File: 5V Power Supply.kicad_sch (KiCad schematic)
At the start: 17 parts, among them Q1 CSD13202Q2, U1 TPS61287RZPR

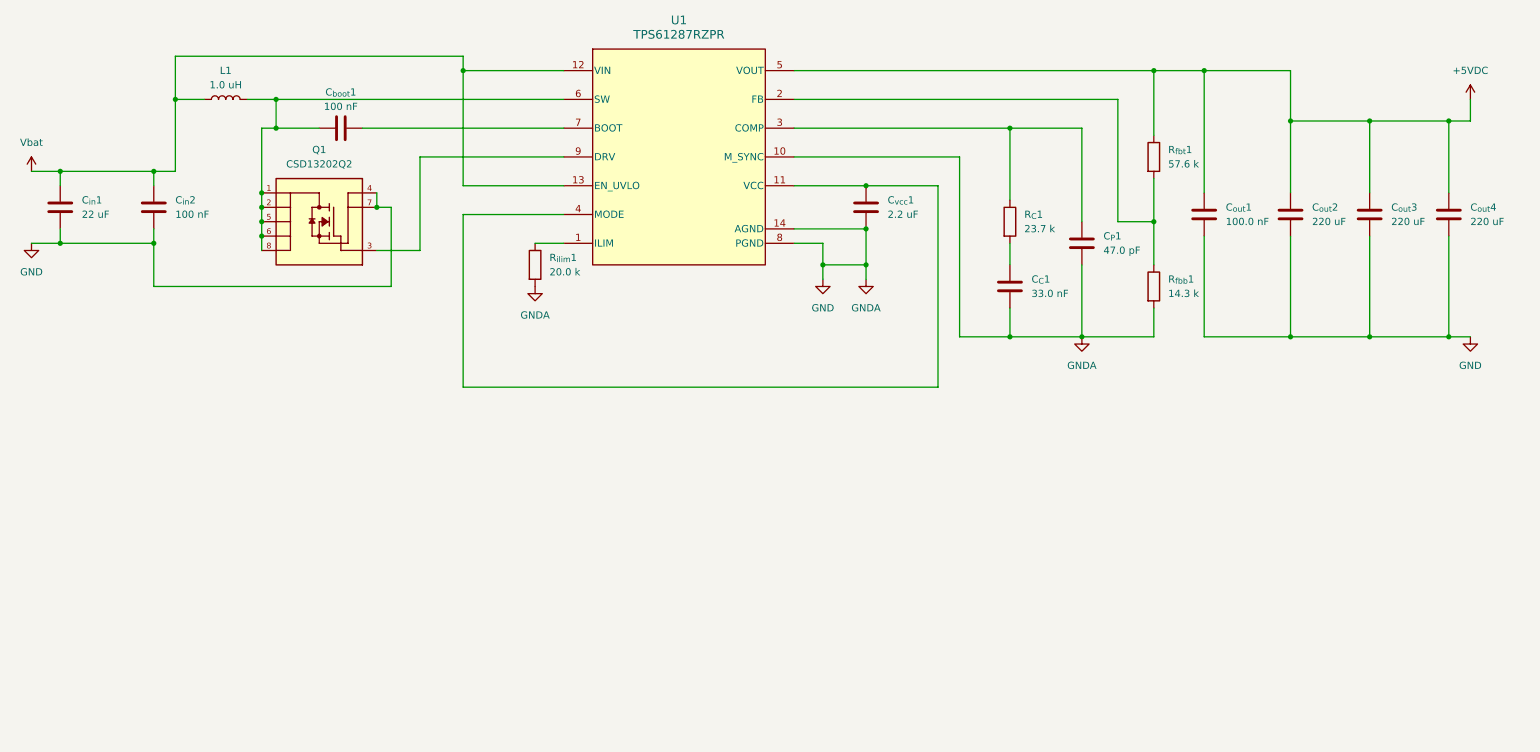
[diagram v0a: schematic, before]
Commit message: feat: Mounting holes, power connectors
Added 2.54 mm ID mounting holes and 4 power connectors. Phoenix Contact spring loaded, good to 16 A, 14-26 AWG wire. 1x on power input from batt, 3x on +5V output.
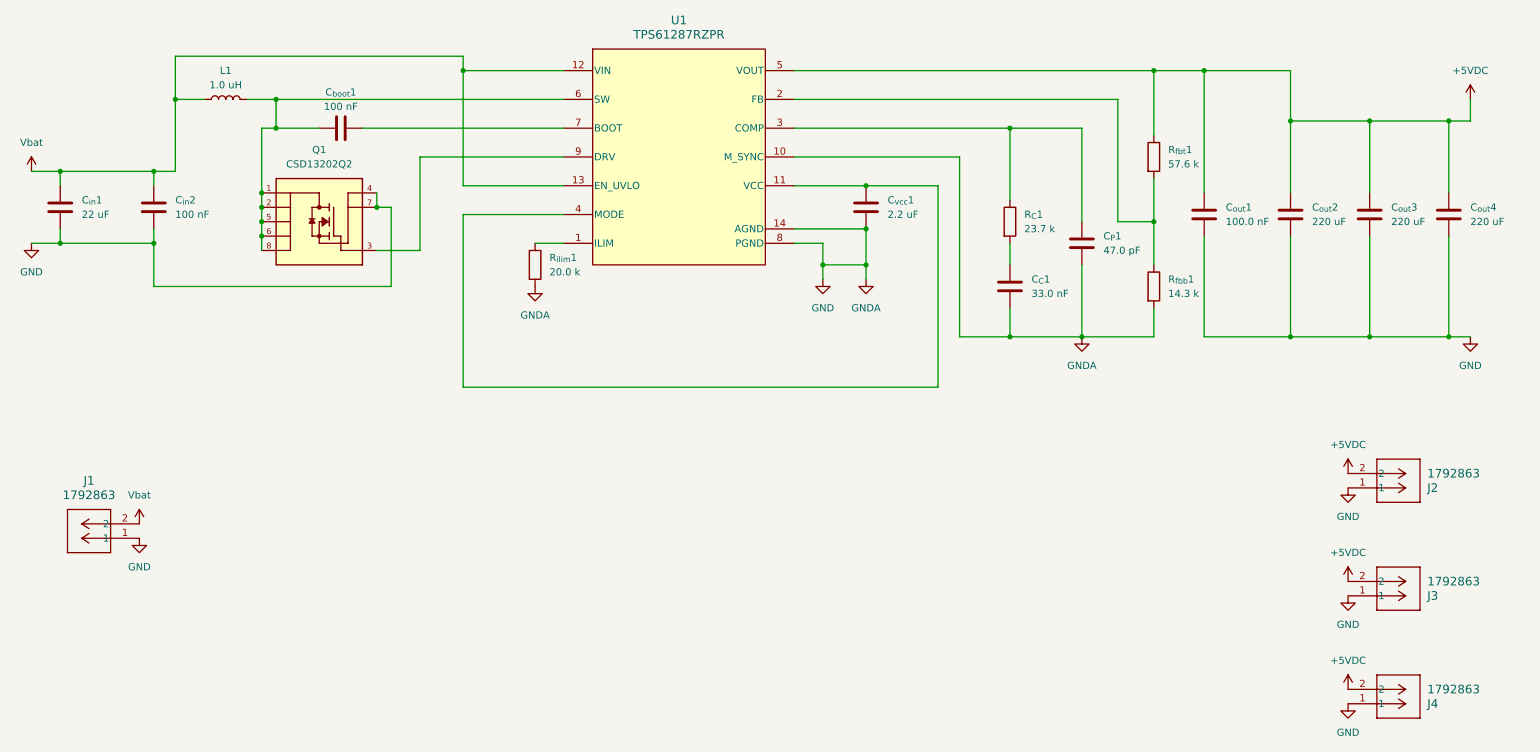
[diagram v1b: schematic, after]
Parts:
- added J1, J2, J3, J4: 1792863, 1792863:CONN_1792863_PXC, symbol 1792863:1792863
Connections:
- net +5VDC: now also J2.2, J3.2, J4.2
- net GND: now also J1.1, J2.1, J3.1, J4.1
- net Vbat: now also J1.2

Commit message: Added test points, silkscreening.
Need to consider input connector. Only rated to 16 A, but at lowest input voltage and highest output current need 18 A on input.
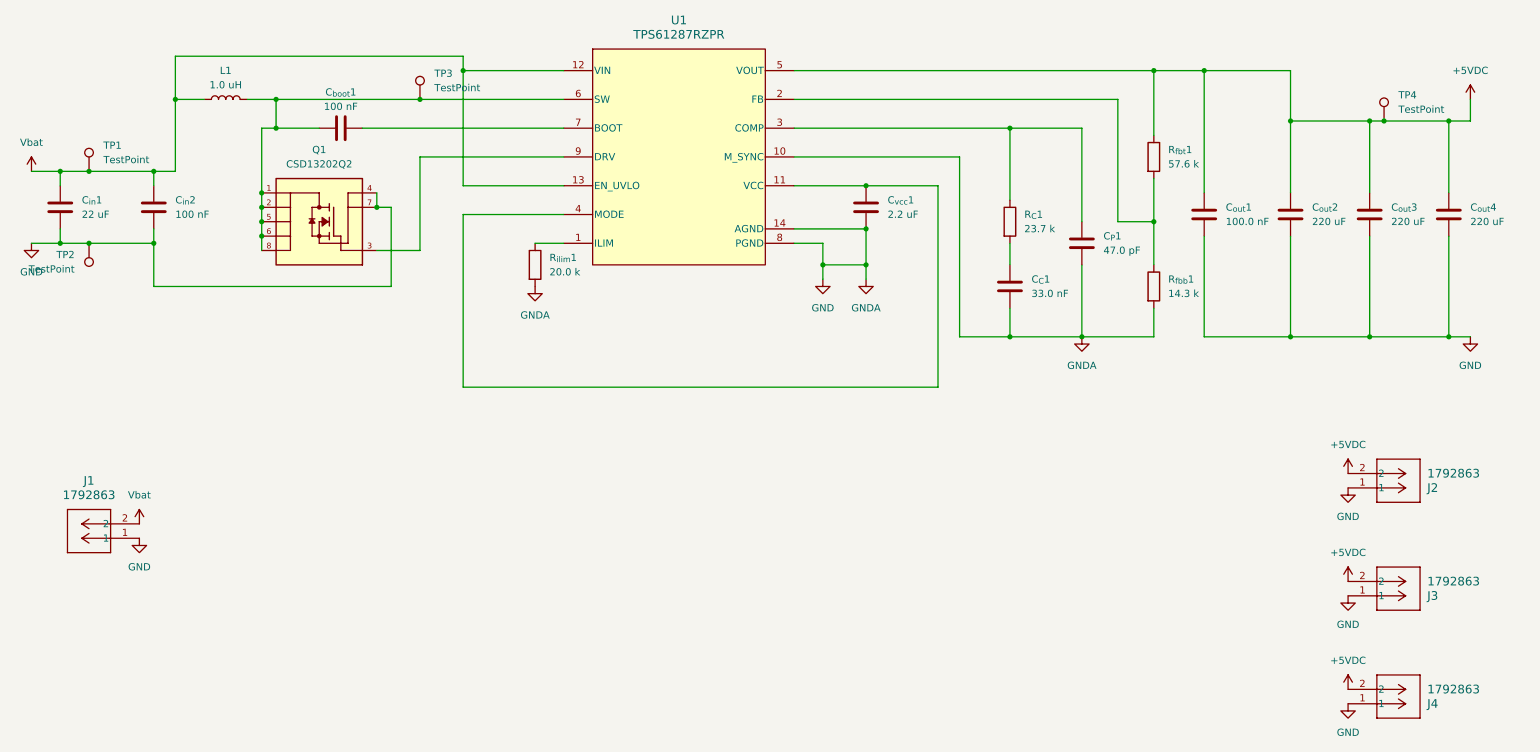
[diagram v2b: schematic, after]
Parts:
- added TP1, TP2, TP3, TP4: TestPoint, TestPoint:TestPoint_THTPad_D1.0mm_Drill0.5mm, symbol Connector:TestPoint
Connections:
- net +5VDC: now also TP4.1
- net GND: now also TP2.1
- net Vbat: now also TP1.1
- net at C_{boot}1.1, L1.2, Q1.1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: now also TP3.1

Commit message: Updated footprints
* Some of the footprints didn't match the size of the part picked for this project.
* Two of the capacitors were swapped.
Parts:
- C_{in}1, C_{vcc}1: footprint Capacitor_SMD:C_0201_0603Metric_Pad0.64x0.40mm_HandSolder -> Capacitor_SMD:C_0603_1608Metric
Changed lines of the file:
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@@
 			)
 		)
-		(property "Footprint" "Capacitor_SMD:C_0201_0603Metric_Pad0.64x0.40mm_HandSolder"
+		(property "Footprint" "Capacitor_SMD:C_0603_1608Metric"
 			(at 26.3652 57.15 0)
 			(effects
@@
 			)
 		)
-		(property "Footprint" "Capacitor_SMD:C_0201_0603Metric_Pad0.64x0.40mm_HandSolder"
+		(property "Footprint" "Capacitor_SMD:C_0603_1608Metric"
 			(at 168.6052 57.15 0)
 			(effects

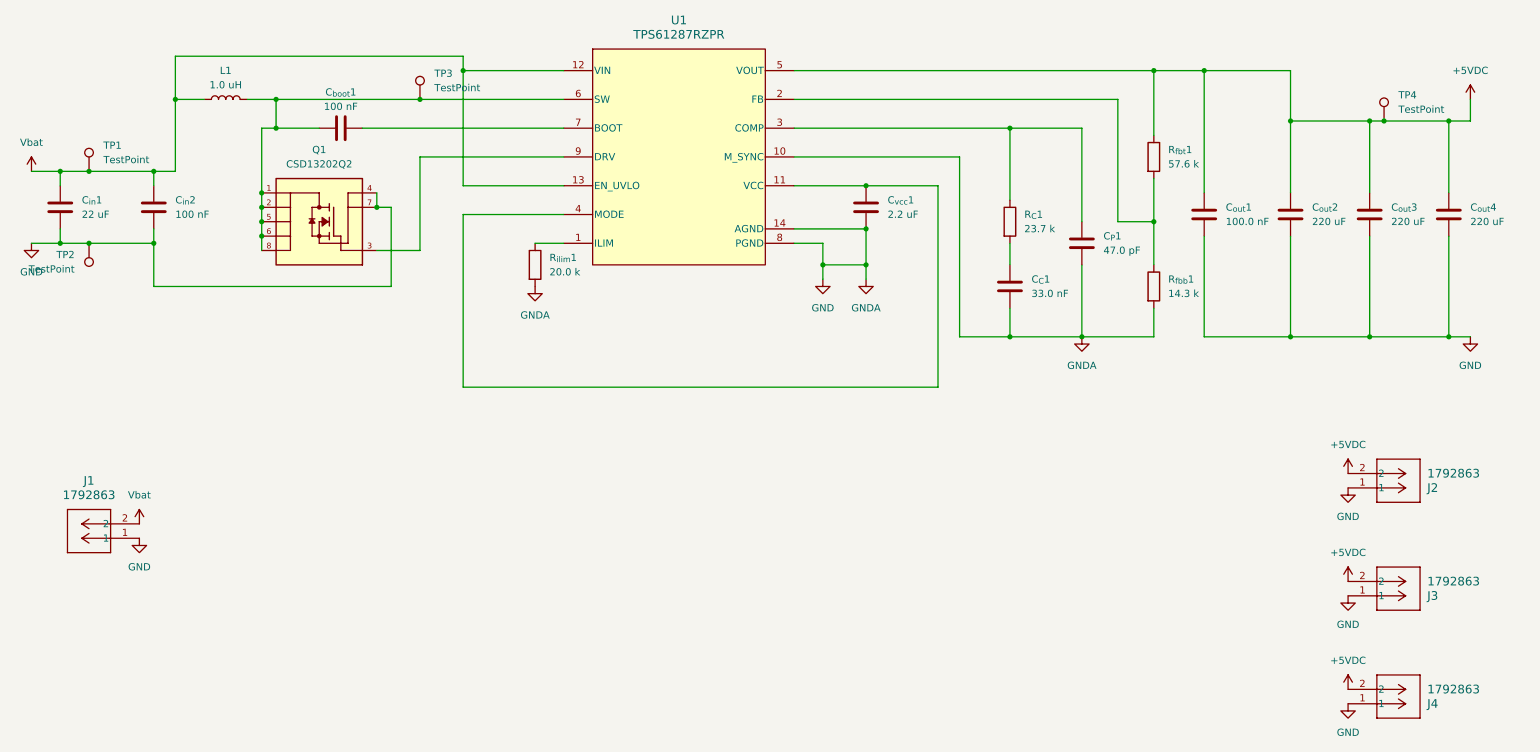
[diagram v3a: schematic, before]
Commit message: feat: Modifications for v1.0
* Removed vias on input GND
* Added test points for measuring voltages. Added in pairs, with 2.5 mm spacing for O-scope spring ground probe
* Removed +5VDC ground pour on bottom layer
* Replaced the two 0201 components with 0402 components
* Adjusted some of the copper pour areas
* Adjusted/added silkscreening
* Moved J1 to get better positioning with top GND copper pour
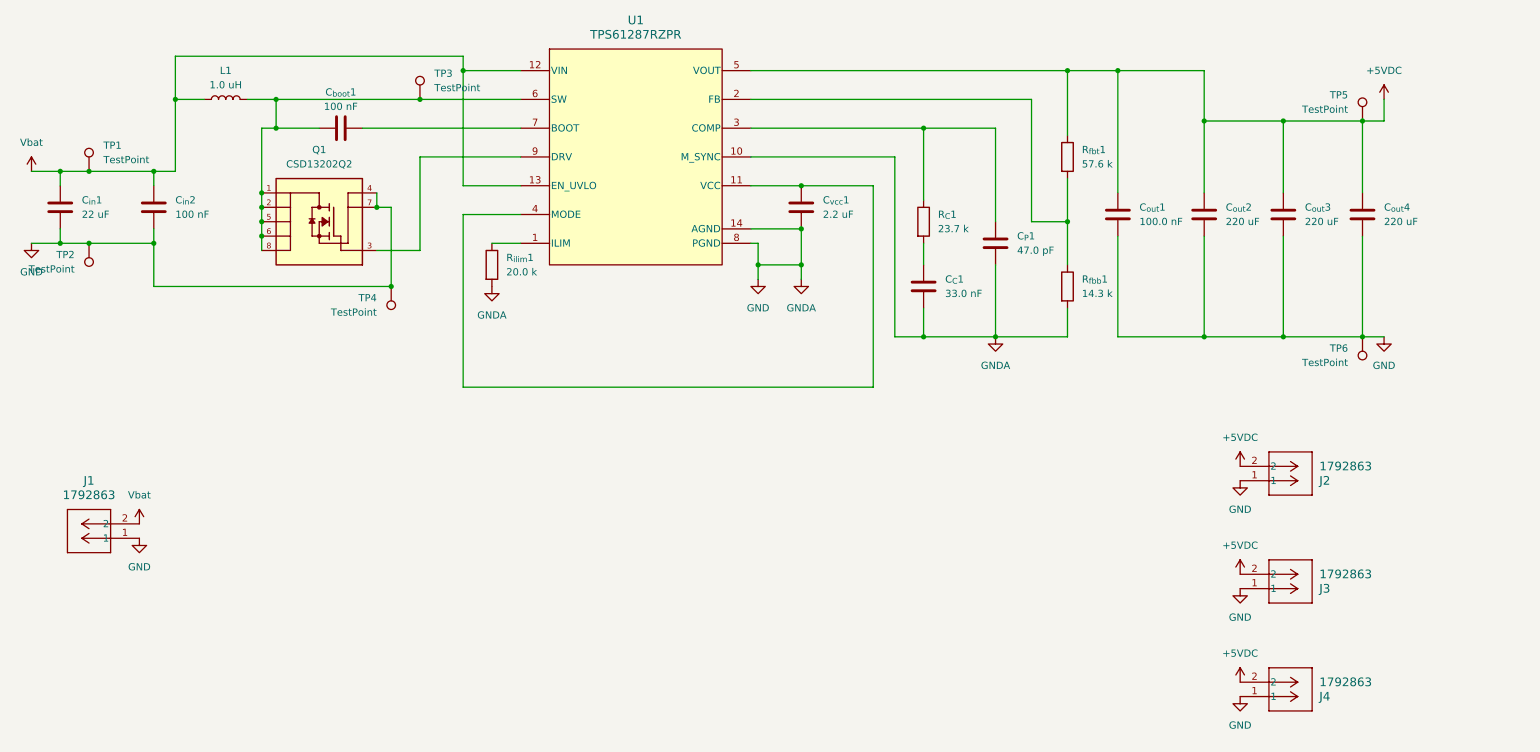
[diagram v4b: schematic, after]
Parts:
- added TP4, TP6: TestPoint, TestPoint:TestPoint_THTPad_D1.0mm_Drill0.5mm, symbol Connector:TestPoint
- C_{C}1: footprint Capacitor_SMD:C_0201_0603Metric_Pad0.64x0.40mm_HandSolder -> Capacitor_SMD:C_0402_1005Metric
- C_{P}1: footprint Capacitor_SMD:C_0805_2012Metric_Pad1.18x1.45mm_HandSolder -> Capacitor_SMD:C_0805_2012Metric
- R_{C}1: footprint Resistor_SMD:R_0201_0603Metric_Pad0.64x0.40mm_HandSolder -> Resistor_SMD:R_0402_1005Metric
- renumbered TP4 to TP5
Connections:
- net GND: now also TP4.1, TP6.1
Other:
- title: (none) -> 5V, 10 A boost supply from 3.0-4.2 VDC input schematic
- moved on the sheet: C_{C}1, C_{P}1, C_{out}1, C_{out}2, C_{out}3, C_{out}4, C_{vcc}1, J2, J3, J4, R_{C}1, R_{fbb}1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
